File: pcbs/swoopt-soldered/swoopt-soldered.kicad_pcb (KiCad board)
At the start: 2 copper layers, 137.6 x 110.1 mm, 91 parts, among them J1 TRRS, SW1 MX, SW10 MX, SW11 MX, SW12 MX, SW13 MX, SW14 MX, SW15 MX, SW16 MX, SW17 MX, SW18 MX, SW19 MX, SW2 MX, SW20 MX, SW21 MX, SW3 MX, SW4 MX, SW5 MX, SW6 MX, SW7 MX, SW8 MX, SW9 MX

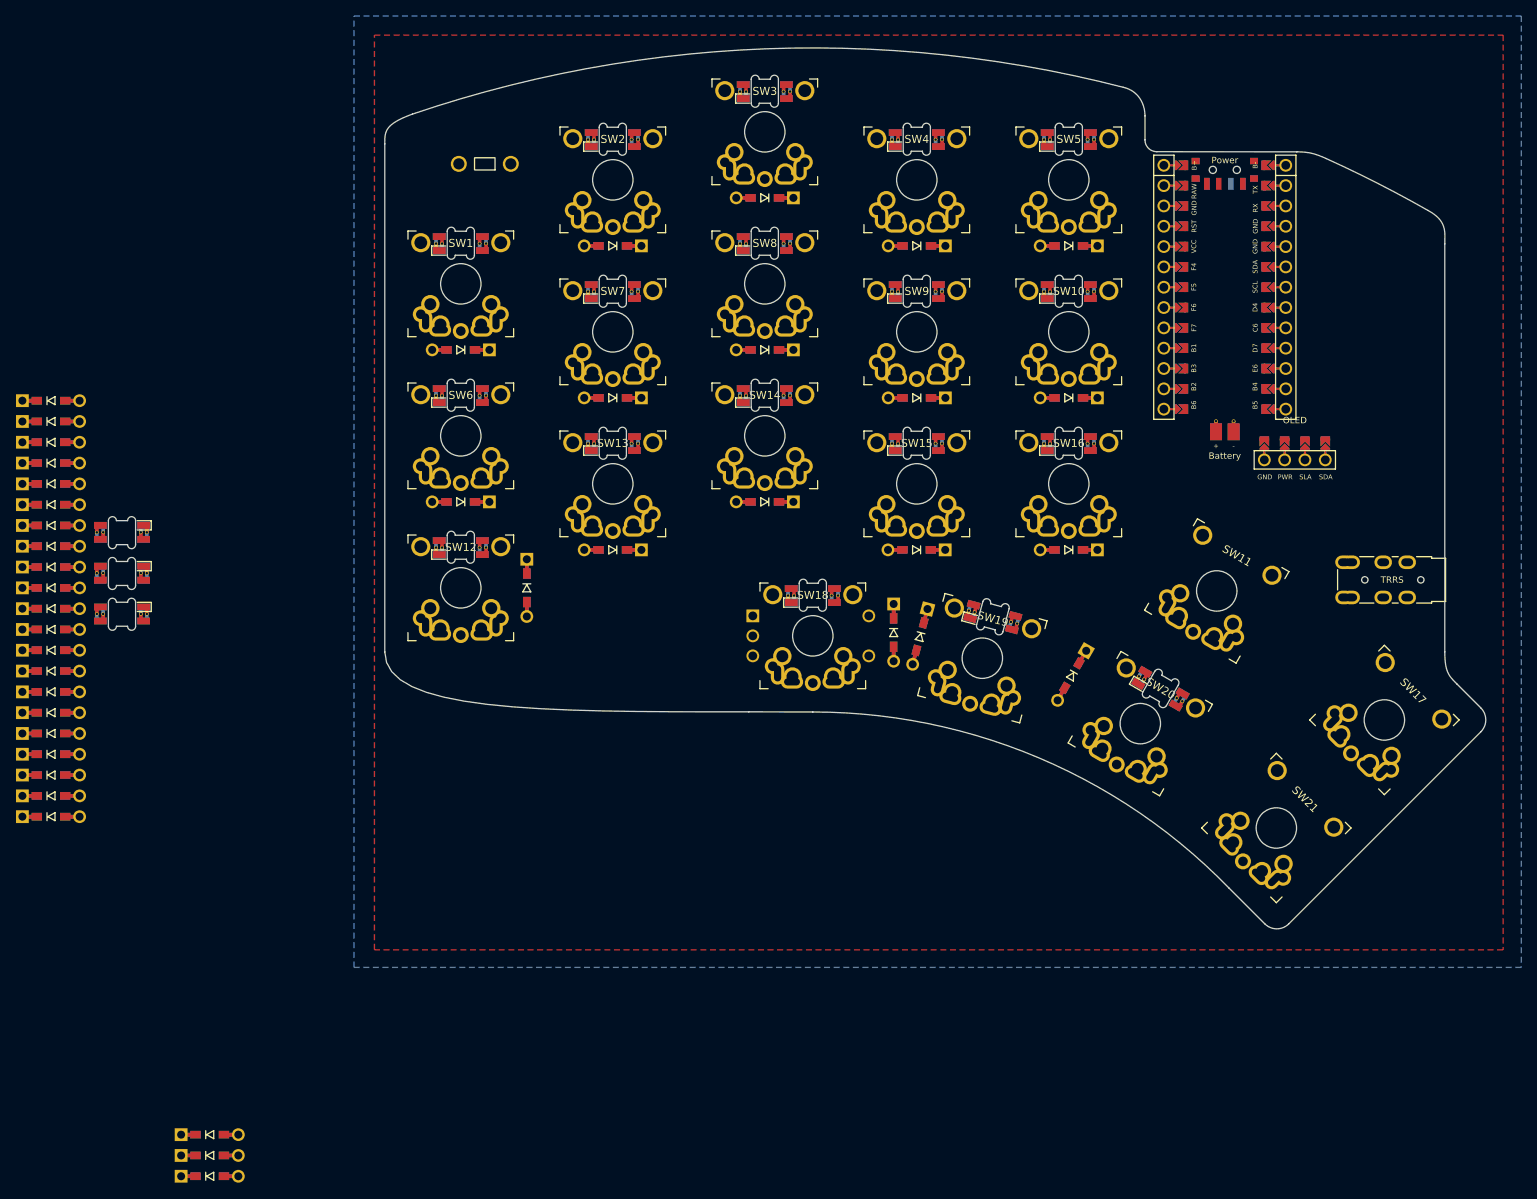
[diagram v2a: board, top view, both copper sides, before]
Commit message: traces are complete, with second jack
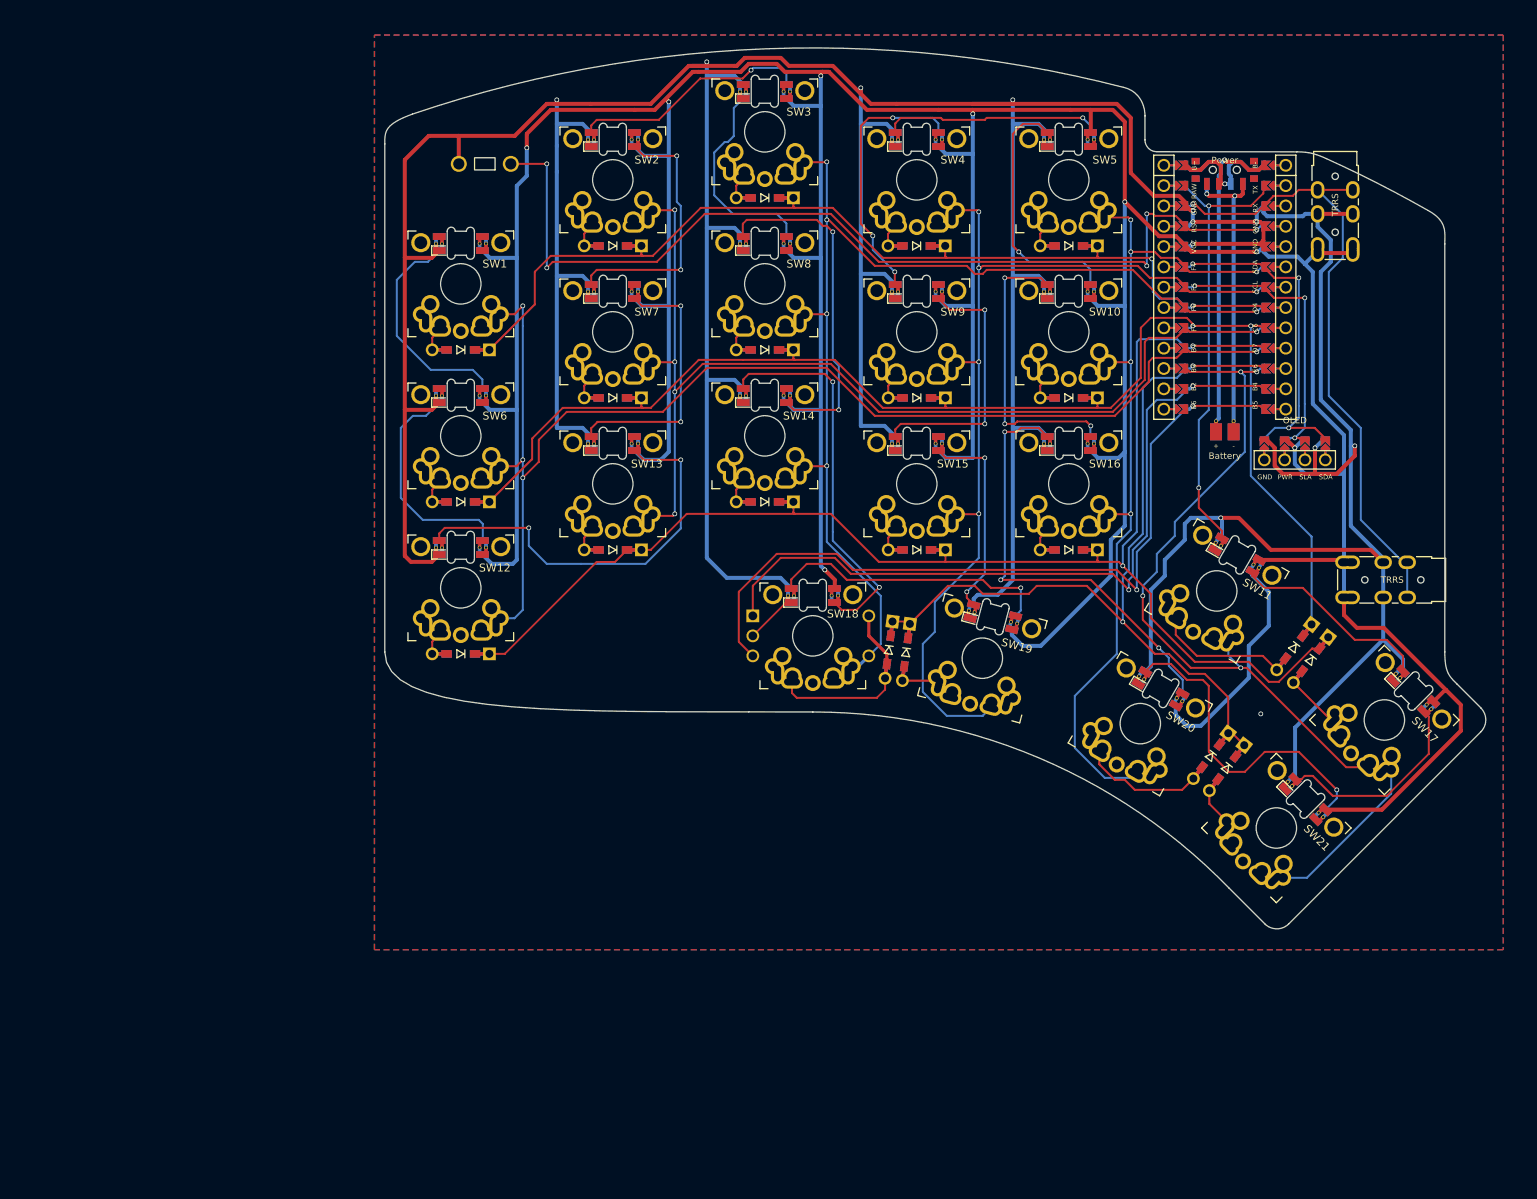
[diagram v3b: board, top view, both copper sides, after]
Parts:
- removed the D1 at (94.0, 81.3)
- removed the D10 at (170.0, 87.3)
- removed the D11 at (102.2, 111.0)
- removed the D12 at (113.0, 106.2)
- removed the D13 at (132.0, 100.2)
- removed the D14 at (151.0, 106.3)
- removed the D15 at (170.0, 106.2)
- removed the D16 at (148.1, 116.6)
- removed the D17 at (151.4, 117.1)
- removed the D18 at (170.4, 122.0)
- removed the D19 at (62.6, 179.3)
- removed the D2 at (113.0, 68.2)
- removed the D20 at (62.6, 181.9)
- removed the D21 at (62.6, 184.5)
- removed the D3 at (132.0, 62.2)
- removed the D4 at (151.0, 68.2)
- removed the D5 at (170.0, 68.3)
- removed the D6 at (94.0, 100.2)
- removed the D7 at (113.0, 87.3)
- removed the D8 at (132.0, 81.2)
- removed the D9 at (151.0, 87.2)
- added J1: TRRS, swoop:TRRS-3pin, F.Cu at (203.3, 58.0)
- moved L17 162.0 mm to (213.0, 124.0), turned to 135 degrees
- moved D17 157.7 mm to (200.2, 120.0), turned to -127.5 degrees
- moved D11 155.5 mm to (198.2, 118.4), turned to -127.5 degrees
- moved L21 149.7 mm to (199.5, 137.5), turned to 135 degrees
- moved D21 147.1 mm to (189.8, 133.5), turned to -127.5 degrees
- moved D20 145.1 mm to (187.8, 132.0), turned to -127.5 degrees
- moved L11 139.4 mm to (191.0, 107.0), turned to 150 degrees
- moved D5 130.7 mm to (170.0, 68.2), turned to 180 degrees
- moved D10 129.4 mm to (170.0, 87.2), turned to 180 degrees
- moved D16 128.8 mm to (170.0, 106.2), turned to 180 degrees
- moved D4 111.6 mm to (151.0, 68.2), turned to 180 degrees
- moved D9 110.3 mm to (151.0, 87.2), turned to 180 degrees
- moved D15 109.7 mm to (151.0, 106.2), turned to 180 degrees
- moved D19 108.0 mm to (149.7, 119.0), turned to -97.5 degrees
- moved D18 105.5 mm to (147.5, 118.8), turned to -97.5 degrees
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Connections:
- L1 pad 2: Net-(L1-DOUT) -> unconnected-(L1-DOUT-Pad2)_1
- L18 pad 2: unconnected-(L18-DOUT-Pad2) -> Net-(L14-DIN)
- L18 pad 4: Net-(L1-DOUT) -> Net-(L18-DIN)
- L19 pad 2: Net-(L14-DIN) -> Net-(L18-DIN)
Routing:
- net GND: track 0.00 -> 676.9 mm, vias 0 -> 12
- net VCC: track 0.00 -> 610.3 mm, vias 0 -> 8
- net row2: track 0.00 -> 171.5 mm, vias 0 -> 2
- net row1: track 0.00 -> 163.8 mm, vias 0 -> 2
- net col0: track 0.00 -> 155.2 mm, vias 0 -> 4
- net col2: track 0.00 -> 135.9 mm, vias 0 -> 5
- net col1: track 0.00 -> 131.5 mm, vias 0 -> 5
- net reset: track 0.00 -> 120.1 mm, vias 0 -> 5
- net row0: track 0.00 -> 120.1 mm, vias 0 -> 2
- net col3: track 0.00 -> 118.6 mm, vias 0 -> 5
- net col5: track 0.00 -> 106.9 mm, vias 0 -> 4
- net col4: track 0.00 -> 105.0 mm, vias 0 -> 5
- net row3: track 0.00 -> 104.4 mm, vias 0 -> 2
- net edb: track 0.00 -> 97.5 mm, vias 0 -> 2
- net eda: track 0.00 -> 93.4 mm, vias 0 -> 2
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- added copper zone on B.Cu, net GND
- added copper zone on F.Cu, net GND
- removed copper zone on B.Cu, net (none)
- removed copper zone on F.Cu, net (none)

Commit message: added underglow leds
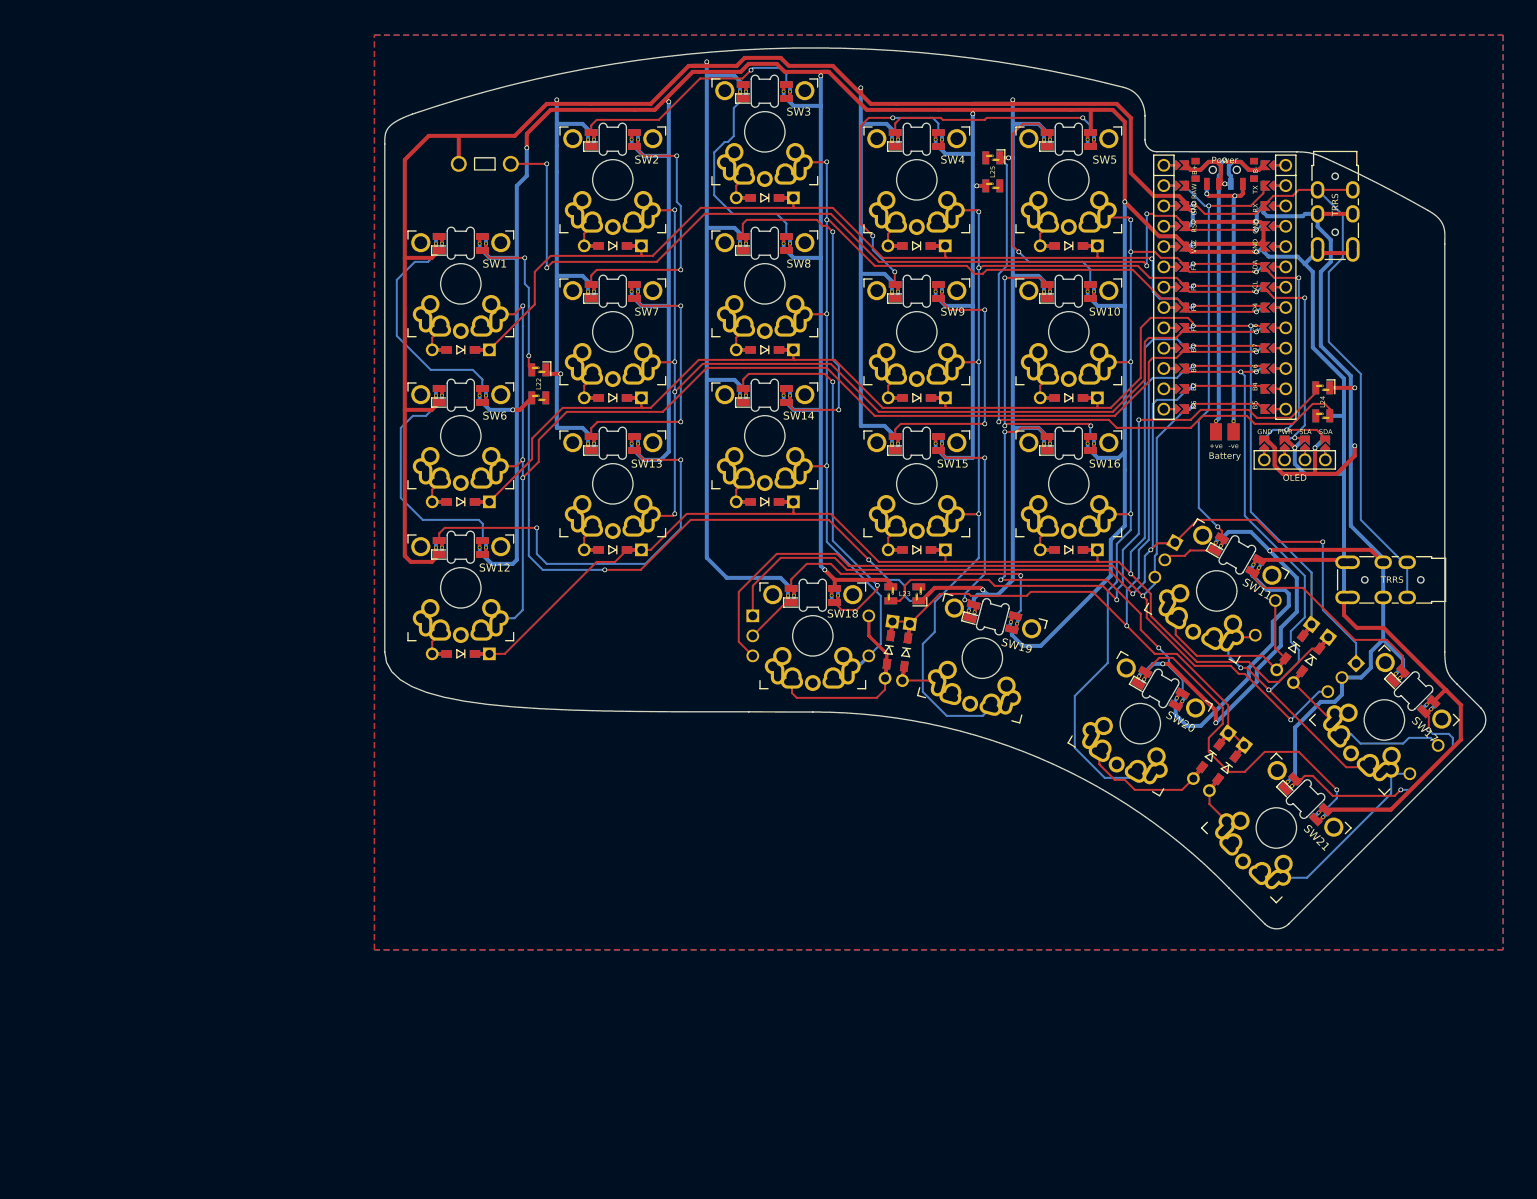
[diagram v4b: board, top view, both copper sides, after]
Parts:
- added EN2: RotaryEncoder_Switch, swoop:RotaryEncoder, F.Cu at (188.5, 111.2)
- added EN3: RotaryEncoder_Switch, swoop:RotaryEncoder, F.Cu at (209.4, 127.5)
- added L22: SK6812Mini-e, diode:LED_SK6812MINI__3.5x3.5mm_reversible, F.Cu at (103.8, 85.5)
- added L23: SK6812Mini-e, diode:LED_SK6812MINI__3.5x3.5mm_reversible, F.Cu at (149.5, 111.8)
- added L24: SK6812Mini-e, diode:LED_SK6812MINI__3.5x3.5mm_reversible, F.Cu at (201.8, 87.8)
- added L25: SK6812Mini-e, diode:LED_SK6812MINI__3.5x3.5mm_reversible, F.Cu at (160.5, 59.0)
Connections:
- net Net-(D11-A) renamed er1
- net Net-(D17-A) renamed er2
- L1 pad 2: unconnected-(L1-DOUT-Pad2)_1 -> Net-(L1-DOUT)
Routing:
- net Net-(L23-DOUT): track 0.00 -> 79.7 mm, vias 0 -> 2
- net Net-(L24-DOUT): track 0.00 -> 78.9 mm, vias 0 -> 1
- net Net-(L22-DOUT): track 0.00 -> 76.9 mm, vias 0 -> 2
- net eda: track 93.4 -> 135.5 mm, vias 2 -> 4
- net GND: track 676.9 -> 715.3 mm, vias 12 -> 17
- net edb: track 97.5 -> 131.7 mm, vias 2 -> 3
- net Net-(L1-DOUT): track 0.00 -> 20.0 mm, vias 0 -> 2
- net VCC: track 610.3 -> 628.2 mm, vias 8 -> 10
- net er2: track 6.96 -> 20.2 mm
- net er1: track 16.2 -> 24.0 mm
- net Net-(L17-DOUT): track 25.7 -> 30.6 mm, vias 0 -> 2
- net row3: track 104.4 -> 102.9 mm
- net Net-(L20-DIN): track 40.8 -> 42.3 mm
- net Net-(L16-DIN): track 54.9 -> 56.0 mm
- net Net-(L18-DIN): track 35.7 -> 36.7 mm
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
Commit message: added tenting screw holes, with needed board alterations
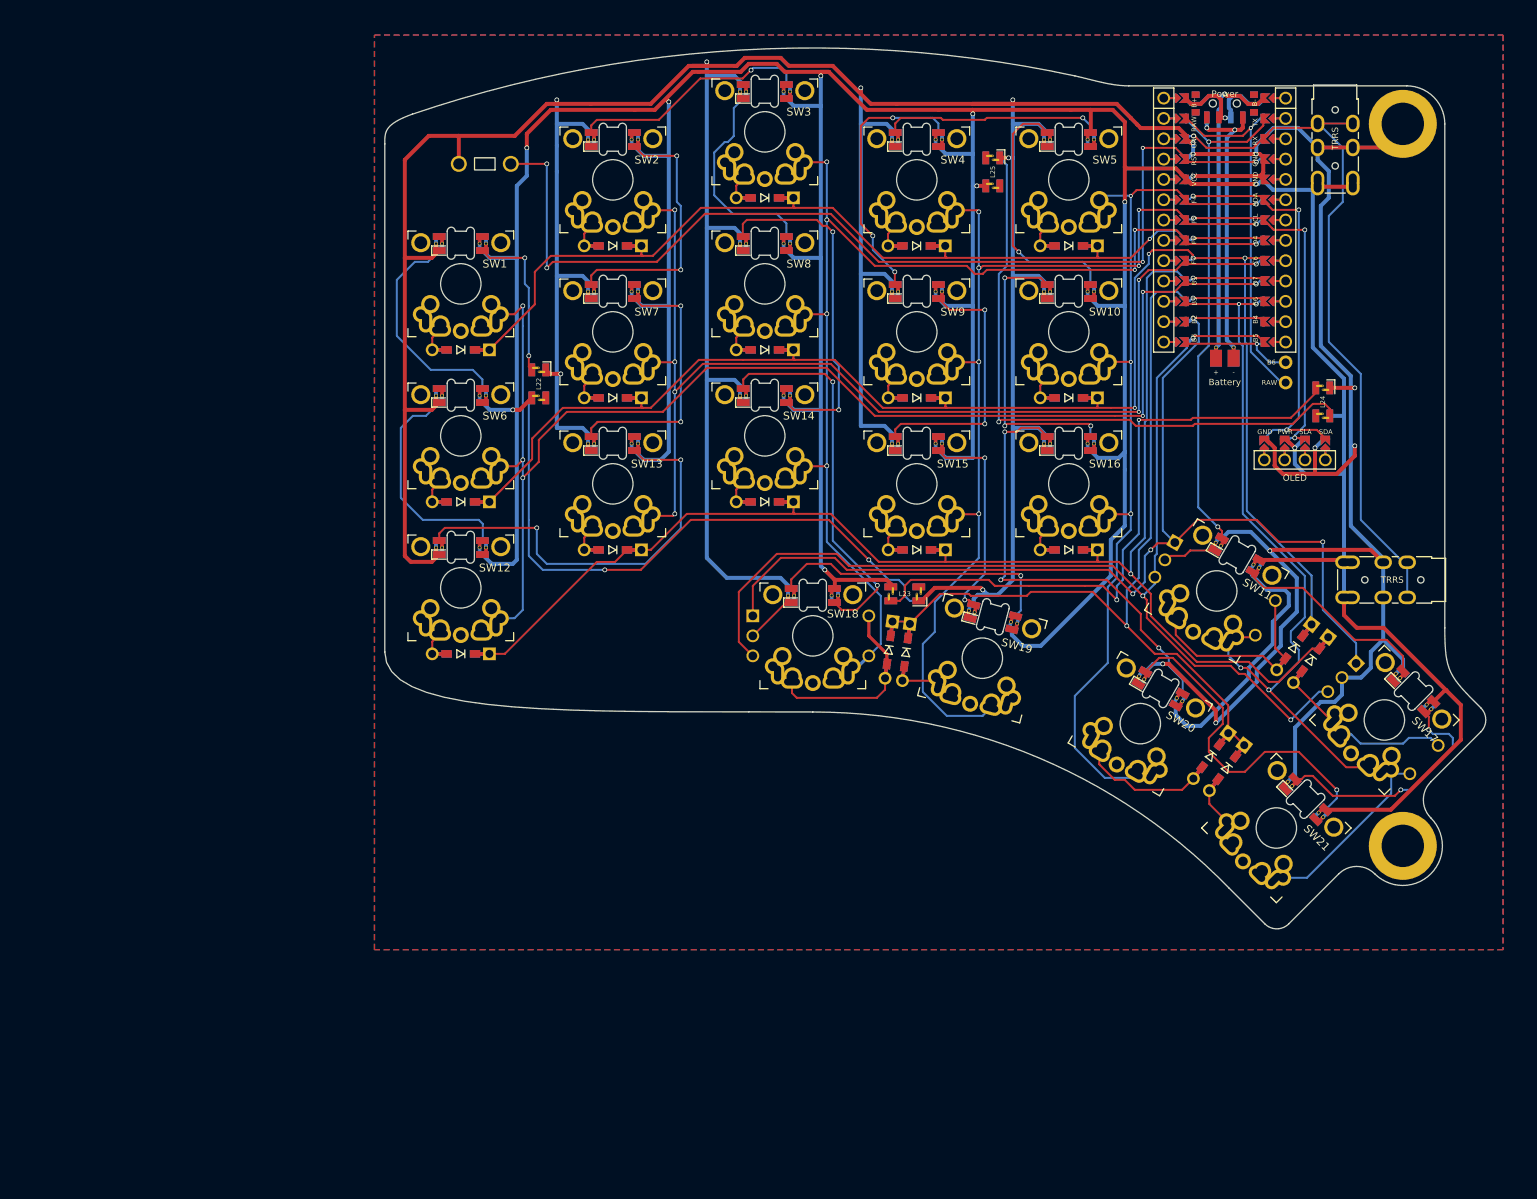
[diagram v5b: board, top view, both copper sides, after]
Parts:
- added REF**: PinSocket_1x02_P2.54mm_Vertical, Connector_PinSocket_2.54mm:PinSocket_1x02_P2.54mm_Vertical, F.Cu at (197.1, 82.8)
- added REF**: MountingHole_5.3mm_M5_ISO14580_Pad, MountingHole:MountingHole_5.3mm_M5_ISO14580_Pad, F.Cu at (211.8, 53.0)
- added REF**: MountingHole_5.3mm_M5_ISO14580_Pad, MountingHole:MountingHole_5.3mm_M5_ISO14580_Pad, F.Cu at (211.8, 143.2)
- U1: moved to B.Cu
- moved BT1 9.20 mm to (189.5, 82.3)
- moved U1 8.40 mm to (189.5, 65.0), turned to 180 degrees
- moved J1 8.30 mm to (203.3, 49.8)
- moved PSW1 8.30 mm to (189.5, 50.5)
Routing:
- net unconnected-(U1-RAW-Pad24): track 0.00 -> 45.2 mm, vias 0 -> 1
- net row1: track 163.9 -> 182.7 mm, vias 2 -> 4
- net unconnected-(U1-B6/10-Pad13): track 0.00 -> 14.6 mm, vias 0 -> 1
- net col0: track 155.2 -> 166.3 mm, vias 4 -> 6
- net row3: track 102.9 -> 113.4 mm
- net col1: track 131.5 -> 141.9 mm, vias 5 -> 7
- net col5: track 106.6 -> 115.2 mm
- net sda: track 43.1 -> 51.7 mm
- net sla: track 36.6 -> 45.1 mm
- net GND: track 715.3 -> 723.9 mm
- net row2: track 170.9 -> 179.4 mm
- net edb: track 131.7 -> 140.2 mm
- net led: track 55.7 -> 64.2 mm
- net data: track 80.0 -> 88.5 mm
- net eda: track 135.5 -> 143.1 mm
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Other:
- outline, holes or cut-outs redrawn
- board text added: "+"
- board text added: "-"
- board text added: "B6"
- board text added: "RAW"
